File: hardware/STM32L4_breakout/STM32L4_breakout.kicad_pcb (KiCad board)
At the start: 2 copper layers, 97.8 x 78.7 mm, 67 parts, among them J1 12V IN, J10 GPIO, J11 SPI1, J12 USART1, J13 USART3, J14 UART4, J15 3.3V, J16 5V, J17 12V, J2 SWD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

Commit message: minor tweaks
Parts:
- moved SW1 7.74 mm to (113.5, 94.2)
- moved J15 6.08 mm to (114.3, 81.8), turned to 180 degrees
- moved J10 5.35 mm to (204.5, 80.0)
- moved J12 5.35 mm to (204.6, 66.7)
- moved J2 5.35 mm to (204.6, 58.4)
- moved J16 4.59 mm to (114.3, 74.7), turned to 180 degrees
- moved J17 4.08 mm to (114.3, 67.6), turned to 180 degrees
- moved J13 2.99 mm to (149.2, 108.7)
- moved J9 2.99 mm to (136.9, 108.7)
- moved J11 2.99 mm to (164.2, 108.8)
- moved J8 2.99 mm to (177.5, 108.7)
- moved J14 2.67 mm to (184.3, 37.3)
- moved J7 2.67 mm to (139.5, 37.3)
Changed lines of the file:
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@@
   )
   (footprint "Connector_PinHeader_2.54mm:PinHeader_1x03_P2.54mm_Vertical" (layer "F.Cu")
-    (at 184.3 40.005 -90)
+    (at 184.3 37.338 -90)
     (descr "Through hole straight pin header, 1x03, 2.54mm pitch, single row")
     (tags "Through hole pin header THT 1x03 2.54mm single row")
@@
   )
   (footprint "Connector_PinHeader_2.54mm:PinHeader_1x03_P2.54mm_Vertical" (layer "F.Cu")
-    (at 199.39 68.04)
+    (at 204.57 66.72)
     (descr "Through hole straight pin header, 1x03, 2.54mm pitch, single row")
     (tags "Through hole pin header THT 1x03 2.54mm single row")
@@
   )
   (footprint "Connector_PinHeader_2.54mm:PinHeader_1x02_P2.54mm_Vertical" (layer "F.Cu")
-    (at 118.375 67.65 90)
+    (at 114.3 67.569 180)
     (descr "Through hole straight pin header, 1x02, 2.54mm pitch, single row")
     (tags "Through hole pin header THT 1x02 2.54mm single row")
@@
     (property "Sheetname" "")
     (attr through_hole)
-    (fp_text reference "J17" (at 1 5.875 180) (layer "F.SilkS")
-      (effects (font (size 1 1) (thickness 0.15)))
-    )
-    (fp_text value "12V" (at -0.7 5.825 180) (layer "F.SilkS")
-      (effects (font (size 1 1) (thickness 0.15)))
-    )
-    (fp_text user "${REFERENCE}" (at 0 1.27) (layer "F.Fab")
+    (fp_text reference "J17" (at -3.506 -1.187 180) (layer "F.SilkS")
+      (effects (font (size 1 1) (thickness 0.15)))
+    )
+    (fp_text value "12V" (at -3.556 0.513 180) (layer "F.SilkS")
+      (effects (font (size 1 1) (thickness 0.15)))
+    )
+    (fp_text user "${REFERENCE}" (at 0 1.27 90) (layer "F.Fab")
       (effects (font (size 1 1) (thickness 0.15)))
     )
@@
     (fp_line (start 1.27 3.81) (end -1.27 3.81) (layer "F.Fab") (width 0.1))
     (fp_line (start -1.27 3.81) (end -1.27 -0.635) (layer "F.Fab") (width 0.1))
-    (pad "1" thru_hole rect (at 0 0 90) (size 1.7 1.7) (drill 1) (layers *.Cu *.Mask)
+    (pad "1" thru_hole rect (at 0 0 180) (size 1.7 1.7) (drill 1) (layers *.Cu *.Mask)
       (net 1 "+12V") (pinfunction "Pin_1") (pintype "passive"))
-    (pad "2" thru_hole oval (at 0 2.54 90) (size 1.7 1.7) (drill 1) (layers *.Cu *.Mask)
+    (pad "2" thru_hole oval (at 0 2.54 180) (size 1.7 1.7) (drill 1) (layers *.Cu *.Mask)
       (net 1 "+12V") (pinfunction "Pin_2") (pintype "passive"))
     (model "${KICAD6_3DMODEL_DIR}/Connector_PinHeader_2.54mm.3dshapes/PinHeader_1x02_P2.54mm_Vertical.wrl"
@@
   )
   (footprint "Connector_PinHeader_2.54mm:PinHeader_1x02_P2.54mm_Vertical" (layer "F.Cu")
-    (at 118.275 72.4 90)
+    (at 114.3 74.686 180)
     (descr "Through hole straight pin header, 1x02, 2.54mm pitch, single row")
     (tags "Through hole pin header THT 1x02 2.54mm single row")
@@
     (property "Sheetname" "")
     (attr through_hole)
-    (fp_text reference "J16" (at 0.8 5.875 180) (layer "F.SilkS")
-      (effects (font (size 1 1) (thickness 0.15)))
-    )
-    (fp_text value "5V" (at -0.9 5.475 180) (layer "F.SilkS")
-      (effects (font (size 1 1) (thickness 0.15)))
-    )
-    (fp_text user "${REFERENCE}" (at 0 1.27) (layer "F.Fab")
+    (fp_text reference "J16" (at -3.556 -1.265 180) (layer "F.SilkS")
+      (effects (font (size 1 1) (thickness 0.15)))
+    )
+    (fp_text value "5V" (at -3.956 0.435 180) (layer "F.SilkS")
+      (effects (font (size 1 1) (thickness 0.15)))
+    )
+    (fp_text user "${REFERENCE}" (at 0 1.27 90) (layer "F.Fab")
       (effects (font (size 1 1) (thickness 0.15)))
     )
@@
     (fp_line (start -1.27 -0.635) (end -0.635 -1.27) (layer "F.Fab") (width 0.1))
     (fp_line (start -1.27 3.81) (end -1.27 -0.635) (layer "F.Fab") (width 0.1))
-    (pad "1" thru_hole rect (at 0 0 90) (size 1.7 1.7) (drill 1) (layers *.Cu *.Mask)
+    (pad "1" thru_hole rect (at 0 0 180) (size 1.7 1.7) (drill 1) (layers *.Cu *.Mask)
       (net 3 "+5V") (pinfunction "Pin_1") (pintype "passive"))
-    (pad "2" thru_hole oval (at 0 2.54 90) (size 1.7 1.7) (drill 1) (layers *.Cu *.Mask)
+    (pad "2" thru_hole oval (at 0 2.54 180) (size 1.7 1.7) (drill 1) (layers *.Cu *.Mask)
       (net 3 "+5V") (pinfunction "Pin_2") (pintype "passive"))
     (model "${KICAD6_3DMODEL_DIR}/Connector_PinHeader_2.54mm.3dshapes/PinHeader_1x02_P2.54mm_Vertical.wrl"
@@
   )
   (footprint "Connector_PinHeader_2.54mm:PinHeader_1x02_P2.54mm_Vertical" (layer "F.Cu")
-    (at 176.525 105.9 90)
+    (at 177.541 108.712 90)
     (descr "Through hole straight pin header, 1x02, 2.54mm pitch, single row")
     (tags "Through hole pin header THT 1x02 2.54mm single row")
@@
   )
   (footprint "Connector_PinHeader_2.54mm:PinHeader_1x06_P2.54mm_Vertical" (layer "F.Cu")
-    (at 199.39 59.69 180)
+    (at 204.57 58.37 180)
     (descr "Through hole straight pin header, 1x06, 2.54mm pitch, single row")
     (tags "Through hole pin header THT 1x06 2.54mm single row")
@@
   )
   (footprint "Button_Switch_SMD:SW_SPDT_PCM12" (layer "F.Cu")
-    (at 113.665 86.5 -90)
+    (at 113.538 94.234 -90)
     (descr "Ultraminiature Surface Mount Slide Switch, right-angle, https://www.ckswitches.com/media/1424/pcm.pdf")
     (property "Sheetfile" "STM32L4_breakout.kicad_sch")
@@
   )
   (footprint "Connector_PinHeader_2.54mm:PinHeader_1x02_P2.54mm_Vertical" (layer "F.Cu")
-    (at 118.275 77.2 90)
+    (at 114.3 81.798 180)
     (descr "Through hole straight pin header, 1x02, 2.54mm pitch, single row")
     (tags "Through hole pin header THT 1x02 2.54mm single row")
@@
     (property "Sheetname" "")
     (attr through_hole)
-    (fp_text reference "J15" (at 0.85 5.825 180) (layer "F.SilkS")
-      (effects (font (size 1 1) (thickness 0.15)))
-    )
-    (fp_text value "3.3V" (at -0.8 6.175 180) (layer "F.SilkS")
-      (effects (font (size 1 1) (thickness 0.15)))
-    )
-    (fp_text user "${REFERENCE}" (at 0 1.27) (layer "F.Fab")
+    (fp_text reference "J15" (at -3.556 -1.265 180) (layer "F.SilkS")
+      (effects (font (size 1 1) (thickness 0.15)))
+    )
+    (fp_text value "3.3V" (at -3.968 0.385 180) (layer "F.SilkS")
+      (effects (font (size 1 1) (thickness 0.15)))
+    )
+    (fp_text user "${REFERENCE}" (at 0 1.27 90) (layer "F.Fab")
       (effects (font (size 1 1) (thickness 0.15)))
     )
@@
     (fp_line (start 1.27 -1.27) (end 1.27 3.81) (layer "F.Fab") (width 0.1))
     (fp_line (start -0.635 -1.27) (end 1.27 -1.27) (layer "F.Fab") (width 0.1))
-    (pad "1" thru_hole rect (at 0 0 90) (size 1.7 1.7) (drill 1) (layers *.Cu *.Mask)
+    (pad "1" thru_hole rect (at 0 0 180) (size 1.7 1.7) (drill 1) (layers *.Cu *.Mask)
       (net 6 "+3.3V") (pinfunction "Pin_1") (pintype "passive"))
-    (pad "2" thru_hole oval (at 0 2.54 90) (size 1.7 1.7) (drill 1) (layers *.Cu *.Mask)
+    (pad "2" thru_hole oval (at 0 2.54 180) (size 1.7 1.7) (drill 1) (layers *.Cu *.Mask)
       (net 6 "+3.3V") (pinfunction "Pin_2") (pintype "passive"))
     (model "${KICAD6_3DMODEL_DIR}/Connector_PinHeader_2.54mm.3dshapes/PinHeader_1x02_P2.54mm_Vertical.wrl"
@@
   )
   (footprint "Connector_PinHeader_2.54mm:PinHeader_1x02_P2.54mm_Vertical" (layer "F.Cu")
-    (at 135.885 105.918 90)
+    (at 136.901 108.73 90)
     (descr "Through hole straight pin header, 1x02, 2.54mm pitch, single row")
     (tags "Through hole pin header THT 1x02 2.54mm single row")
@@
   )
   (footprint "Connector_PinHeader_2.54mm:PinHeader_1x03_P2.54mm_Vertical" (layer "F.Cu")
-    (at 148.225 105.85 90)
+    (at 149.241 108.662 90)
     (descr "Through hole straight pin header, 1x03, 2.54mm pitch, single row")
     (tags "Through hole pin header THT 1x03 2.54mm single row")
@@
   )
   (footprint "Connector_PinHeader_2.54mm:PinHeader_1x03_P2.54mm_Vertical" (layer "F.Cu")
-    (at 163.175 106 90)
+    (at 164.191 108.812 90)
     (descr "Through hole straight pin header, 1x03, 2.54mm pitch, single row")
     (tags "Through hole pin header THT 1x03 2.54mm single row")
@@
   )
   (footprint "Connector_PinHeader_2.54mm:PinHeader_1x02_P2.54mm_Vertical" (layer "F.Cu")
-    (at 139.525 39.95 90)
+    (at 139.525 37.283 90)
     (descr "Through hole straight pin header, 1x02, 2.54mm pitch, single row")
     (tags "Through hole pin header THT 1x02 2.54mm single row")
@@
   )
   (footprint "Connector_PinHeader_2.54mm:PinHeader_1x09_P2.54mm_Vertical" (layer "F.Cu")
-    (at 199.29 81.34)
+    (at 204.47 80.02)
     (descr "Through hole straight pin header, 1x09, 2.54mm pitch, single row")
     (tags "Through hole pin header THT 1x09 2.54mm single row")

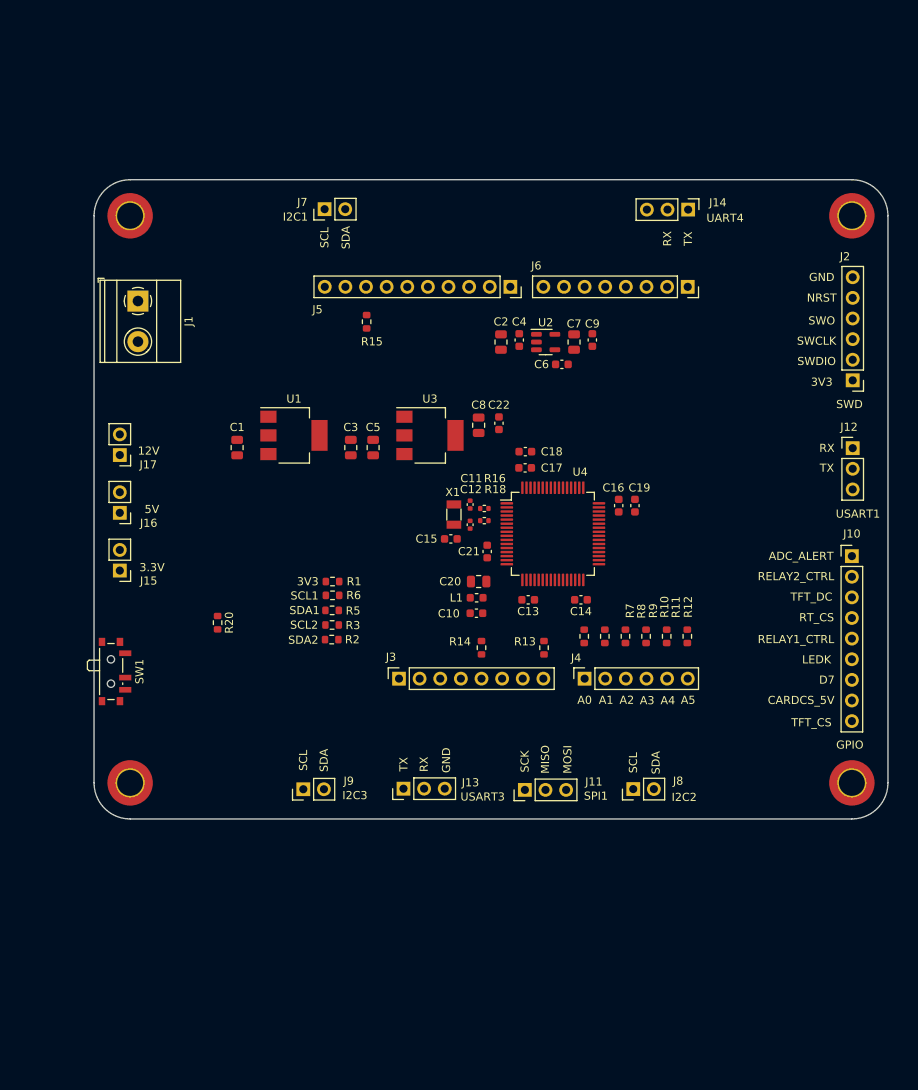
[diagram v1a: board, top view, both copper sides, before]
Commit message: routed mcu caps and clock - SPI lines need move
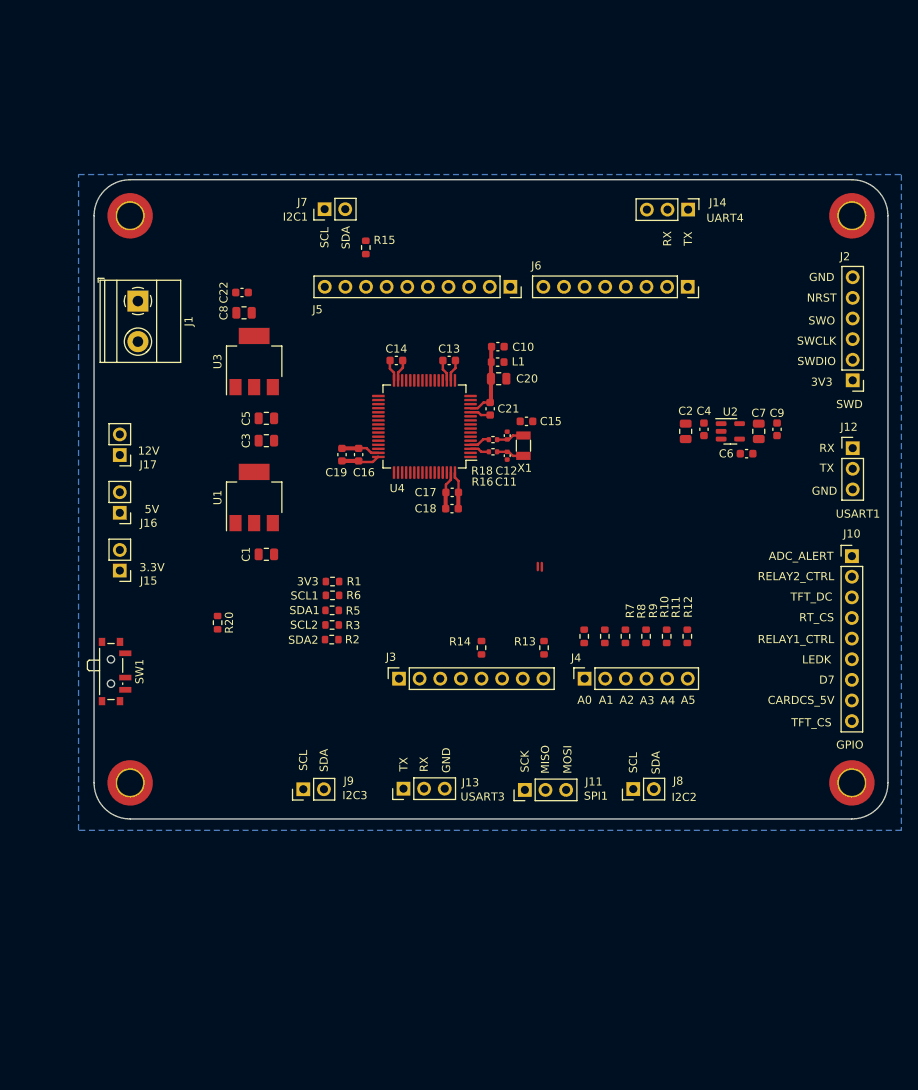
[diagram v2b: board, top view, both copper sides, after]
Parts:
- moved C14 37.2 mm to (148.4, 55.9), turned to 0 degrees
- moved C19 36.6 mm to (141.7, 67.5)
- moved C22 35.5 mm to (129.3, 47.5), turned to 180 degrees
- moved C10 32.9 mm to (160.9, 54.2)
- moved C16 32.6 mm to (143.7, 67.5), turned to 90 degrees
- moved C8 32.0 mm to (129.6, 50.0), turned to 180 degrees
- moved C13 31.0 mm to (154.9, 55.9), turned to 0 degrees
- moved L1 29.1 mm to (160.8, 56.1)
- moved C2 25.3 mm to (184.0, 64.7)
- moved C4 25.3 mm to (186.2, 64.4)
- moved C6 25.3 mm to (191.5, 67.4)
- moved C7 25.3 mm to (193.0, 64.7)
- moved C9 25.3 mm to (195.2, 64.4)
- moved U2 25.3 mm to (189.5, 64.7)
- moved C20 25.1 mm to (161.0, 58.2), turned to 0 degrees
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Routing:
- net GND: track 0.00 -> 18.4 mm
- net +3.3V: track 0.00 -> 15.7 mm
- net +3.3VA: track 0.00 -> 9.65 mm
- net /CRYSTAL_OUT: track 0.00 -> 3.45 mm
- net /CRYSTAL_IN: track 0.00 -> 3.45 mm
- net OSC32OUT: track 0.00 -> 2.56 mm
- net OSC32IN: track 0.00 -> 2.41 mm
- added copper zone on B.Cu, net GND

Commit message: re-arrange pcb layout for SPI lines WIP
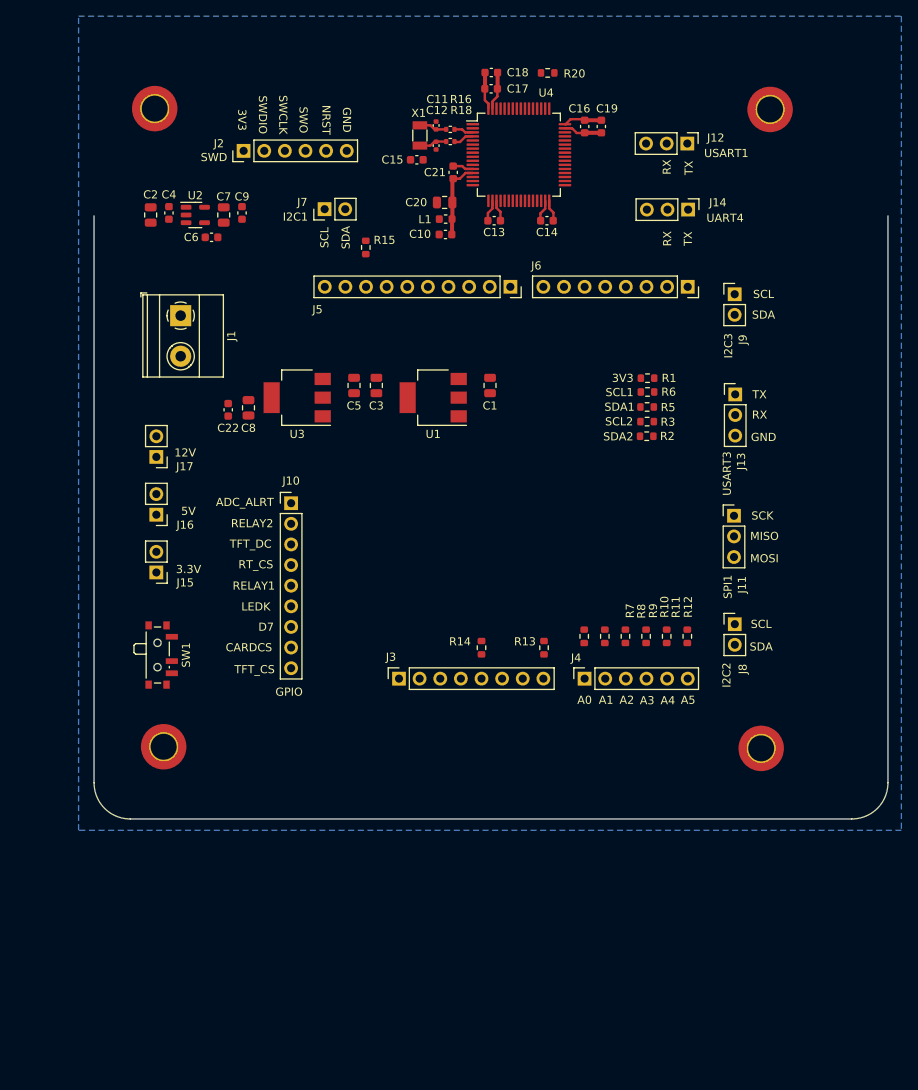
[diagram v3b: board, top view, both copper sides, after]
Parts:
- moved J9 80.9 mm to (190.0, 47.8), turned to 0 degrees
- moved J2 80.2 mm to (129.6, 30.1), turned to 90 degrees
- moved R20 79.0 mm to (167.0, 20.5), turned to 180 degrees
- moved C2 71.1 mm to (118.1, 38.0)
- moved C4 71.1 mm to (120.3, 37.8)
- moved C6 71.1 mm to (125.6, 40.8)
- moved C7 71.1 mm to (127.1, 38.0)
- moved C9 71.1 mm to (129.3, 37.8)
- moved U2 71.1 mm to (123.6, 38.0)
- moved J10 69.4 mm to (135.4, 73.5)
- moved J13 63.5 mm to (190.1, 60.1), turned to 0 degrees
- moved C18 53.9 mm to (160.1, 20.5), turned to 0 degrees
- moved C19 51.5 mm to (173.6, 27.1), turned to -90 degrees
- moved C17 49.9 mm to (160.0, 22.5), turned to 0 degrees
- moved C16 49.1 mm to (171.6, 27.1), turned to -90 degrees
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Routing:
- net +3.3V: track 15.7 -> 14.8 mm
- net GND: track 18.4 -> 17.5 mm
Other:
- board size 97.8 x 78.7 mm -> 97.8 x 74.3 mm

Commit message: re-drew outline based on SPI move
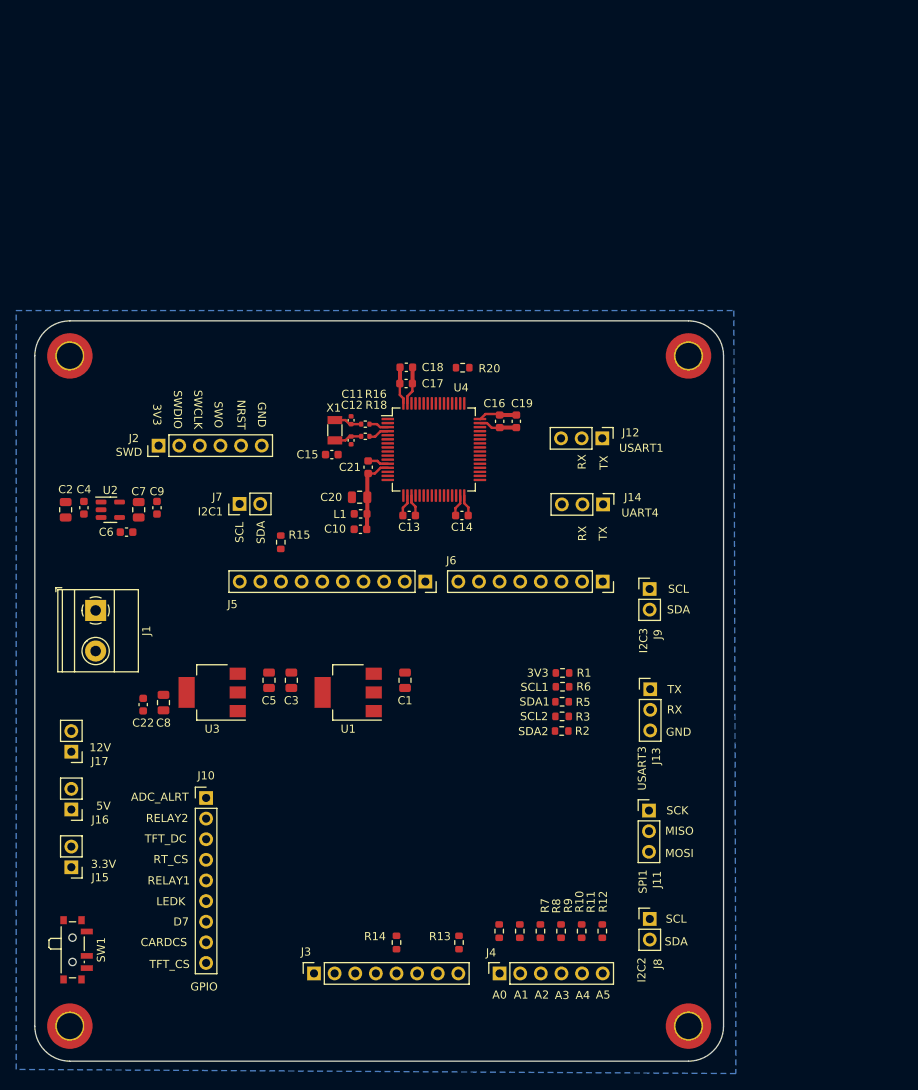
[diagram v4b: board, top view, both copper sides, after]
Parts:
- moved C17 37.8 mm to (149.6, 58.8)
- moved C18 37.8 mm to (149.6, 56.8)
- moved J1 37.8 mm to (111.3, 86.7)
- moved J13 37.8 mm to (179.6, 96.4)
- moved J14 37.8 mm to (173.8, 73.6)
- moved J2 37.8 mm to (119.1, 66.4)
- moved J3 37.8 mm to (138.2, 131.4)
- moved J4 37.8 mm to (161.1, 131.4)
- moved J5 37.8 mm to (151.9, 83.2)
- moved J6 37.8 mm to (173.8, 83.2)
- moved J9 37.8 mm to (179.6, 84.1)
- moved R1 37.8 mm to (168.8, 94.4)
- moved R5 37.8 mm to (168.8, 98.0)
- moved C1 37.8 mm to (149.4, 95.3)
- moved C10 37.8 mm to (143.9, 76.7)
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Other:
- board size 97.8 x 74.3 mm -> 84.8 x 91.2 mm
